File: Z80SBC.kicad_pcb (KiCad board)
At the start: 2 copper layers, 208 x 115 mm, 127 parts, among them IC1 DART-DIP-40, IC2 Z80CPU-DIP, J1 PH, J10 Conn_01x01, J11 Conn_01x01, J12 Conn_01x01, J13 Conn_01x04, J14 RCAJack, J15 Conn_02x04_Odd_Even, J2 DB9_Female, J3 CFCONN, J4 Barrel_Jack, J5 Conn_01x10, J6 Conn_01x10, J7 Conn_01x10, J8 Conn_01x08, J9 Conn_01x01, P1 Mini-DIN_6pins_ver4, Q1 2N3906, SW1 SW_Push, SW2 SW_Push, U1 MAX232_ALT, U10 74HCT32, U11 74HCT00, U12 74HC393, U13 74HC595pwr, U14 74HC165, U15 MicroSD_SPI_CD, U16 MicroSD_SPI_CD, U2 74LS138, U3 628128, U4 28C256, U5 LM7805, U6 74HCT32, U7 74HCT00, U8 74HCT32, U9 8255A, Y1 7.3728 MHz, Y2 16 MHz

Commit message: Fixed SDHC support, added extra configuration jumpers
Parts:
- U11, U7: value 74HCT00 -> 74HC00
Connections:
- U11 pad 10: +5V -> Net-(C18-Pad1)
- U11 pad 12: +5V -> SCK
- U11 pad 2: +5V -> Net-(C13-Pad1)
- U7 pad 5: +5V -> Net-(C6-Pad1)
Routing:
- net +5V: track 1129.0 -> 1105.5 mm, vias 21 -> 20
- net Net-(C18-Pad1): track 25.6 -> 28.5 mm
- net Net-(C6-Pad1): track 26.6 -> 29.3 mm
- net SCK: track 205.2 -> 207.8 mm
- net Net-(C13-Pad1): track 10.1 -> 12.6 mm
- net Net-(U11-Pad11): track 149.6 -> 148.5 mm
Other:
- board text added: "74HC00"
- board text added: "DAN'S Z80 SBC V2 LAYOUT BY DANIEL MARKS PCB COPYRIGHT LICENSE CC-BY-SA 4.0"
- board text removed: "74HCT00"
- board text removed: "Z80 SBC V2 LAYOUT BY DANIEL MARKS"

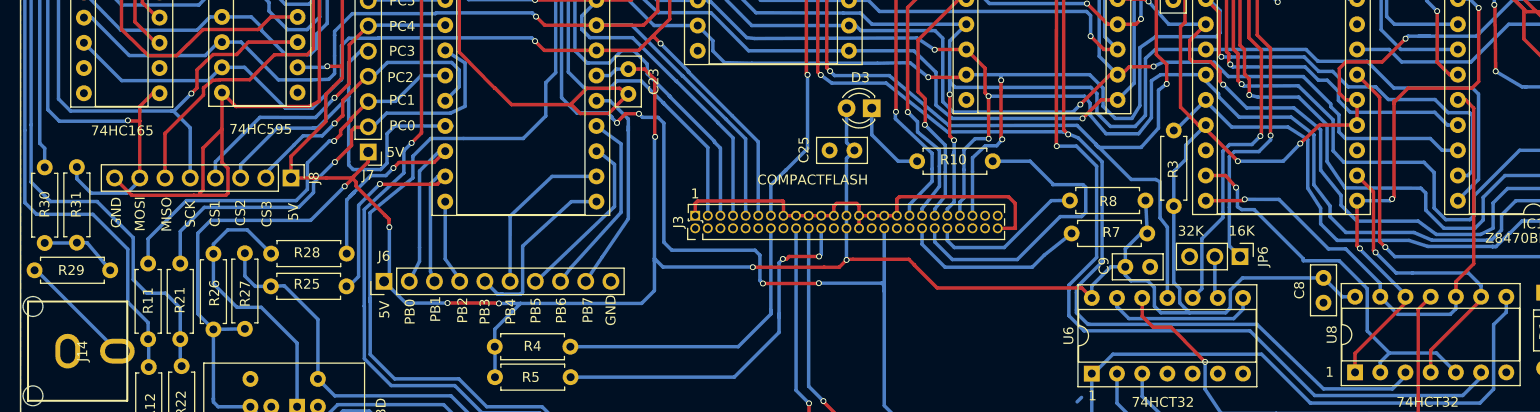
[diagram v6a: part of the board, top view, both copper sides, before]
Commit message: Modified video output
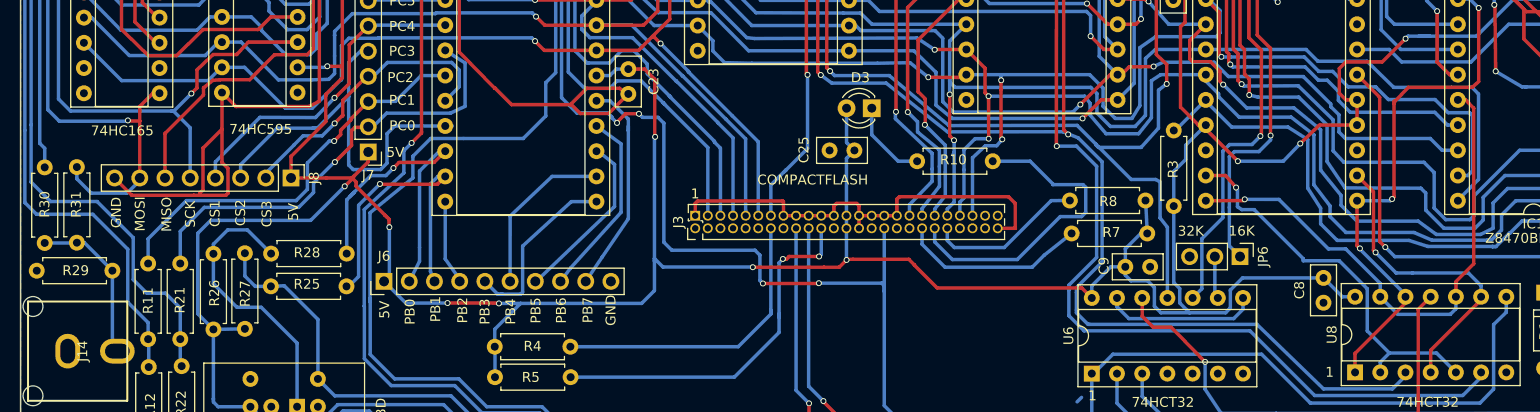
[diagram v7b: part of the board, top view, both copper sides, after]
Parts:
- R29: value 82R -> 100R
- moved R29 7.84 mm to (28.2, 117.5), turned to 180 degrees
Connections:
- R29 pad 2: Net-(R29-Pad2) -> GND
- R30 pad 1: Net-(R29-Pad2) -> Net-(J14-Pad2)
- R31 pad 1: Net-(R29-Pad2) -> Net-(J14-Pad2)
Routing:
- net Net-(R29-Pad2): track 7.91 -> 0.00 mm
- net Net-(J14-Pad2): track 11.7 -> 16.3 mm

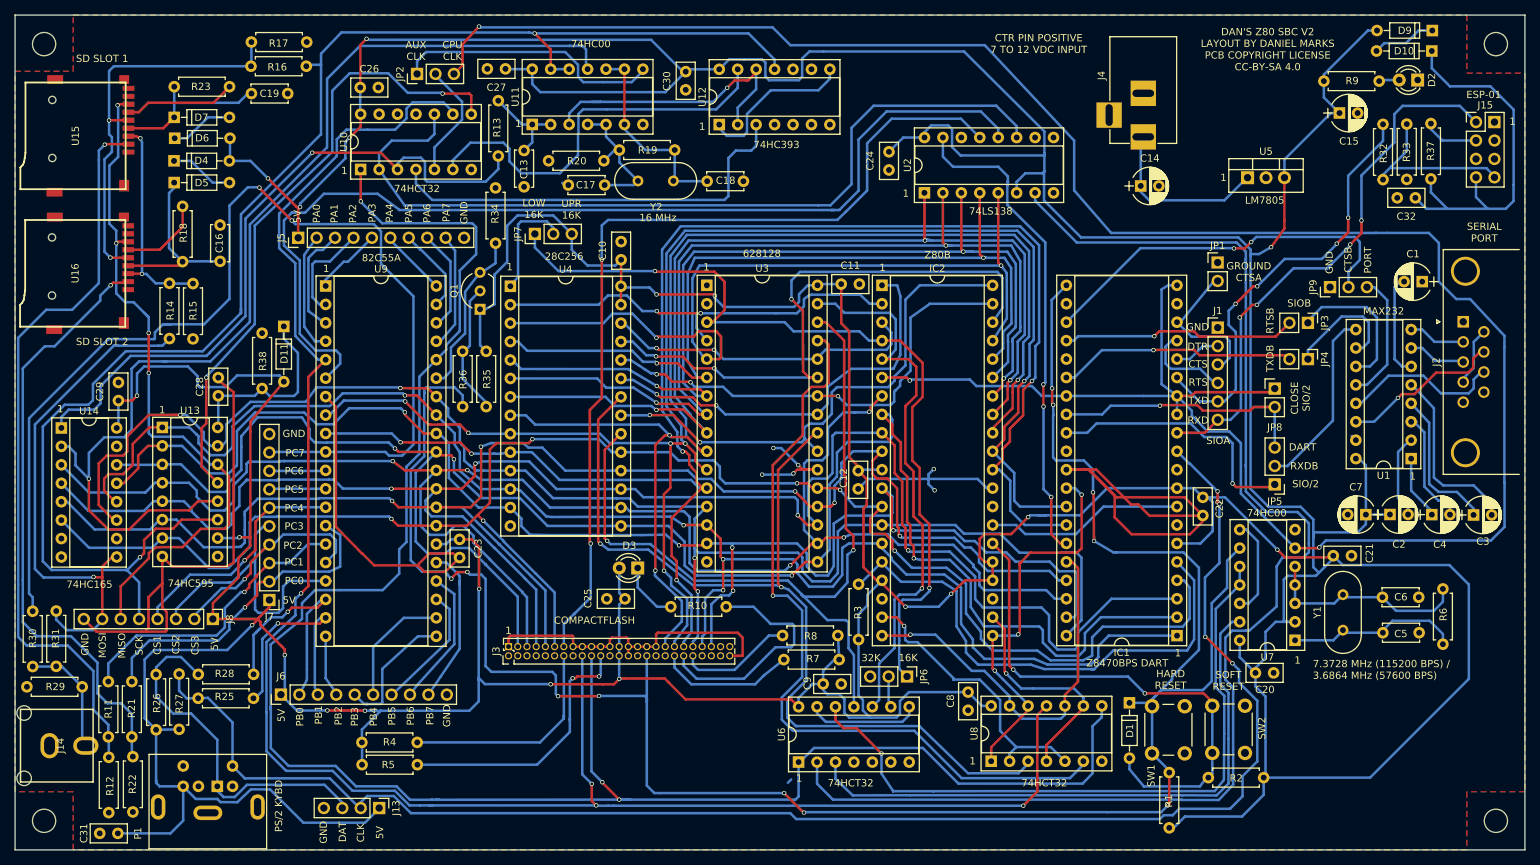
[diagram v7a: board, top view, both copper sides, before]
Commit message: Moved around port B/C pins to separate input and output groups
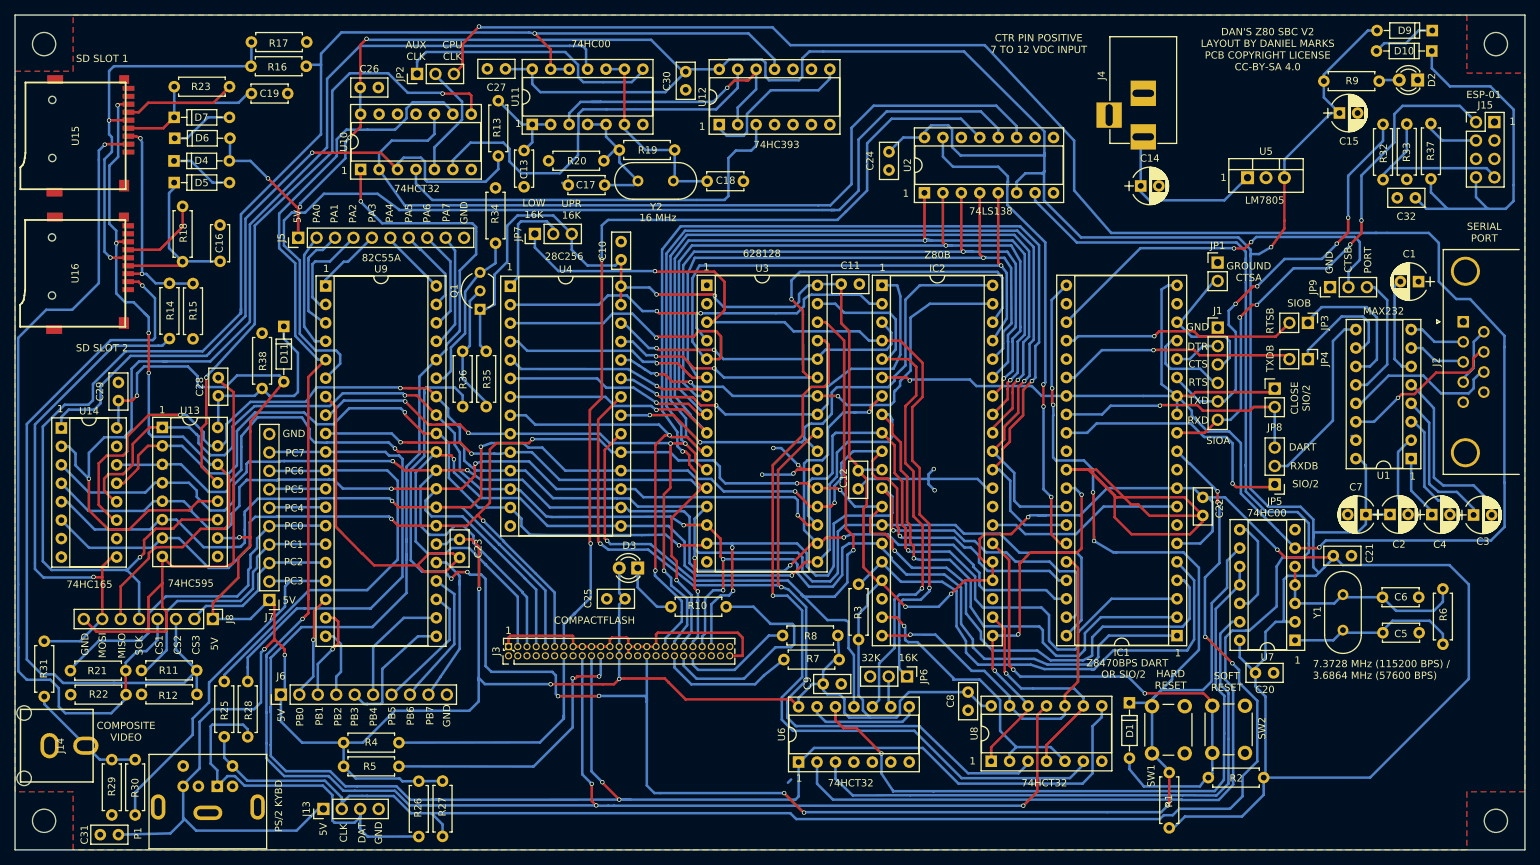
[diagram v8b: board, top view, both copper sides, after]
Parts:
- R29: value 100R -> NC
- moved R27 42.6 mm to (77.9, 138.1), turned to 90 degrees
- moved R26 42.5 mm to (74.6, 138.2), turned to 90 degrees
- moved R30 19.1 mm to (35.5, 127.6), turned to 270 degrees
- moved R22 18.3 mm to (26.7, 118.6), turned to 0 degrees
- moved R12 16.9 mm to (36.4, 118.6), turned to 0 degrees
- moved R28 11.0 mm to (51.0, 124.4), turned to 90 degrees
- moved R29 10.8 mm to (32.3, 127.6), turned to 270 degrees
- moved R21 8.59 mm to (26.6, 115.3), turned to 0 degrees
- moved J13 7.69 mm to (61.5, 134.4), turned to 90 degrees
- moved R25 6.42 mm to (47.8, 124.4), turned to 90 degrees
- moved R11 4.81 mm to (36.4, 115.3), turned to 0 degrees
- moved R31 4.48 mm to (23.0, 118.9)
- moved R5 2.55 mm to (64.3, 128.5)
- moved R4 2.52 mm to (64.3, 125.2)
- moved C1 0.51 mm to (212.3, 61.7)
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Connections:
- J7 pad 3: Net-(J7-Pad3) -> SDCS3
- J7 pad 4: CS3 -> Net-(J7-Pad4)
- J7 pad 5: CS2 -> Net-(J7-Pad5)
- J7 pad 6: CS1 -> Net-(J7-Pad6)
- J8 pad 2: CS3 -> SDCS3
- J8 pad 3: CS2 -> SDCS2
- J8 pad 4: CS1 -> SDCS
- R11 pad 1: Net-(J7-Pad3) -> Net-(J7-Pad4)
- R11 pad 2: SDCS -> SDCS2
- R12 pad 2: SDCS -> SDCS2
- R21 pad 1: Net-(J7-Pad2) -> Net-(J7-Pad5)
- R21 pad 2: SDCS2 -> SDCS
- R22 pad 2: SDCS2 -> SDCS
- R25 pad 2: Net-(J6-Pad3) -> Net-(J7-Pad8)
- R28 pad 2: Net-(J6-Pad2) -> Net-(J7-Pad9)
- R30 pad 2: Net-(J7-Pad9) -> Net-(J7-Pad2)
- U9 pad 13: CS1 -> Net-(J7-Pad6)
- U9 pad 14: Net-(J7-Pad2) -> Net-(J7-Pad5)
- U9 pad 15: Net-(J7-Pad3) -> Net-(J7-Pad4)
- U9 pad 16: CS3 -> SDCS3
- U9 pad 17: CS2 -> Net-(J7-Pad2)
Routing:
- net Net-(J7-Pad9): track 152.0 -> 64.3 mm, vias 2 -> 0
- net Net-(J7-Pad8): track 8.22 -> 61.1 mm
- net Net-(J7-Pad5): track 0.00 -> 48.2 mm
- net CS2: track 43.0 -> 0.00 mm
- net Net-(J7-Pad3): track 41.2 -> 0.00 mm, vias 1 -> 0
- net Net-(J7-Pad4): track 0.00 -> 37.9 mm
- net CS1: track 33.5 -> 0.00 mm, vias 1 -> 0
- net CS3: track 29.5 -> 0.00 mm, vias 1 -> 0
- net SDCS3: track 0.00 -> 22.7 mm
- net SDCS2: track 83.5 -> 102.6 mm
- net Net-(J6-Pad3): track 30.5 -> 13.2 mm
- net Net-(J6-Pad2): track 32.9 -> 15.7 mm
- net SDCS: track 103.3 -> 116.0 mm
- net SYNCA: track 218.3 -> 209.4 mm
- net +5V: track 1105.5 -> 1096.8 mm, vias 20 -> 18
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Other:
- board text added: "COMPOSITE VIDEO"
- board text added: "OR SIO/2"
